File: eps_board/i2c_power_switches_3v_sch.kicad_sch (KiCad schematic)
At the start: 10 parts, among them U34 MCP23017T-E/SS

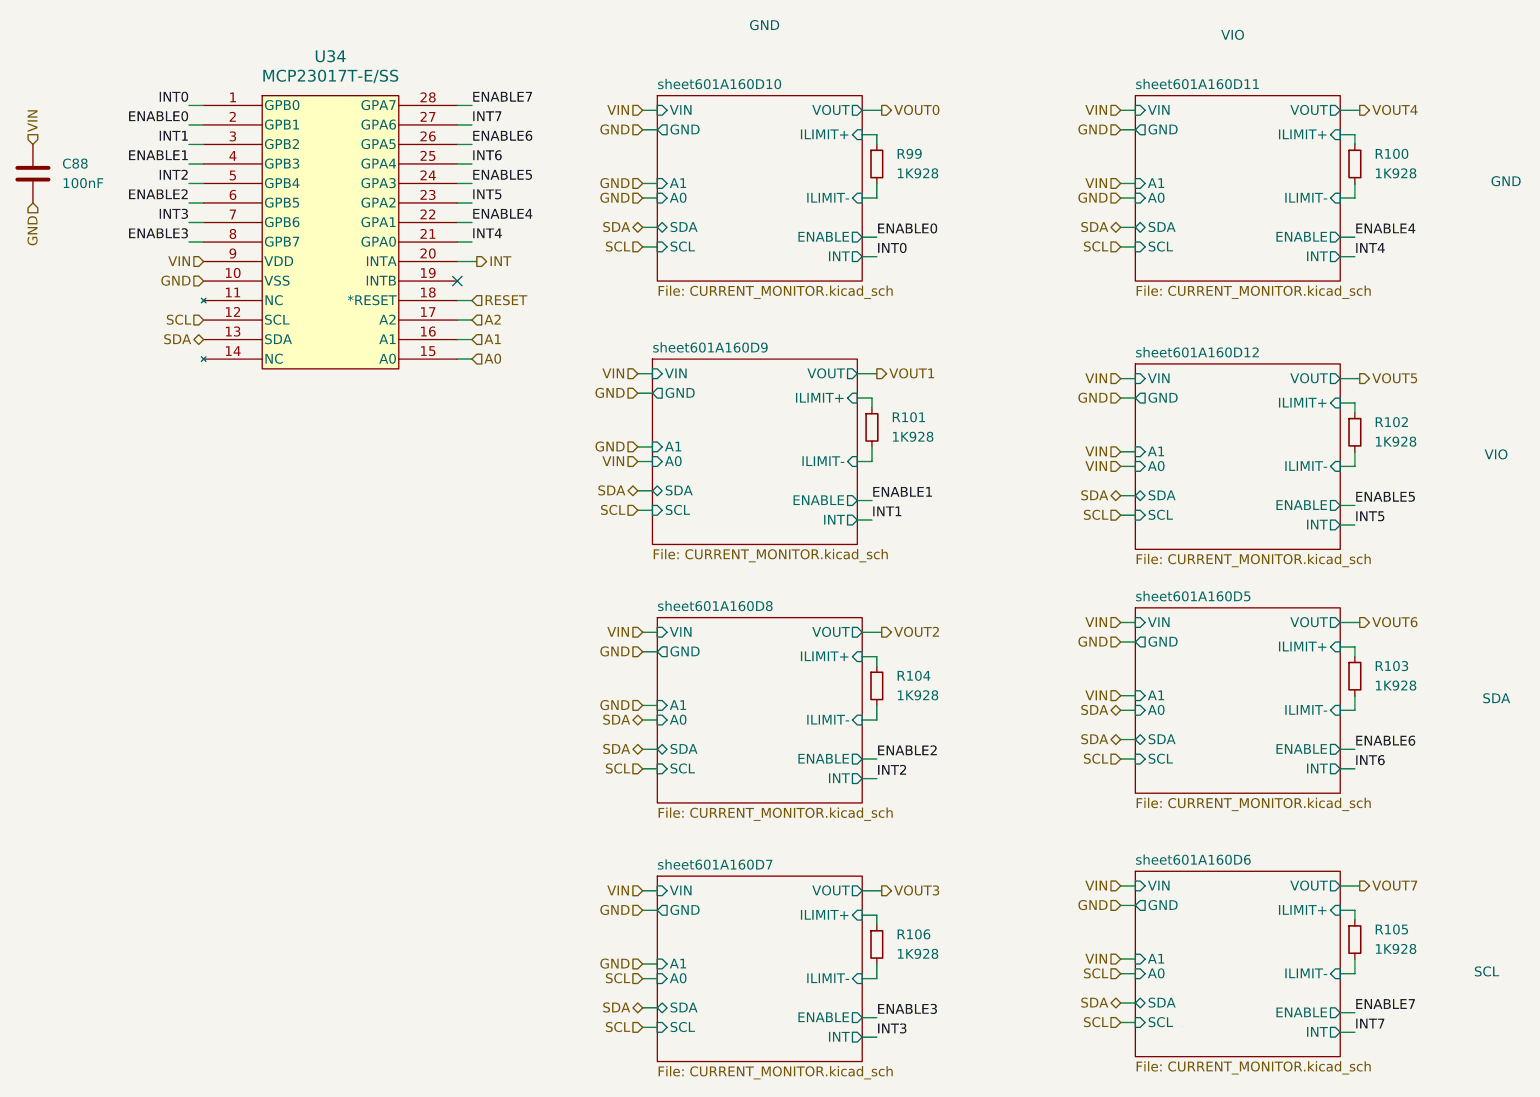
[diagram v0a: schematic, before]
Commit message: cleaning up bom: remove main camera port since it has not pullups and capacitors, correcting some errors in camera switch
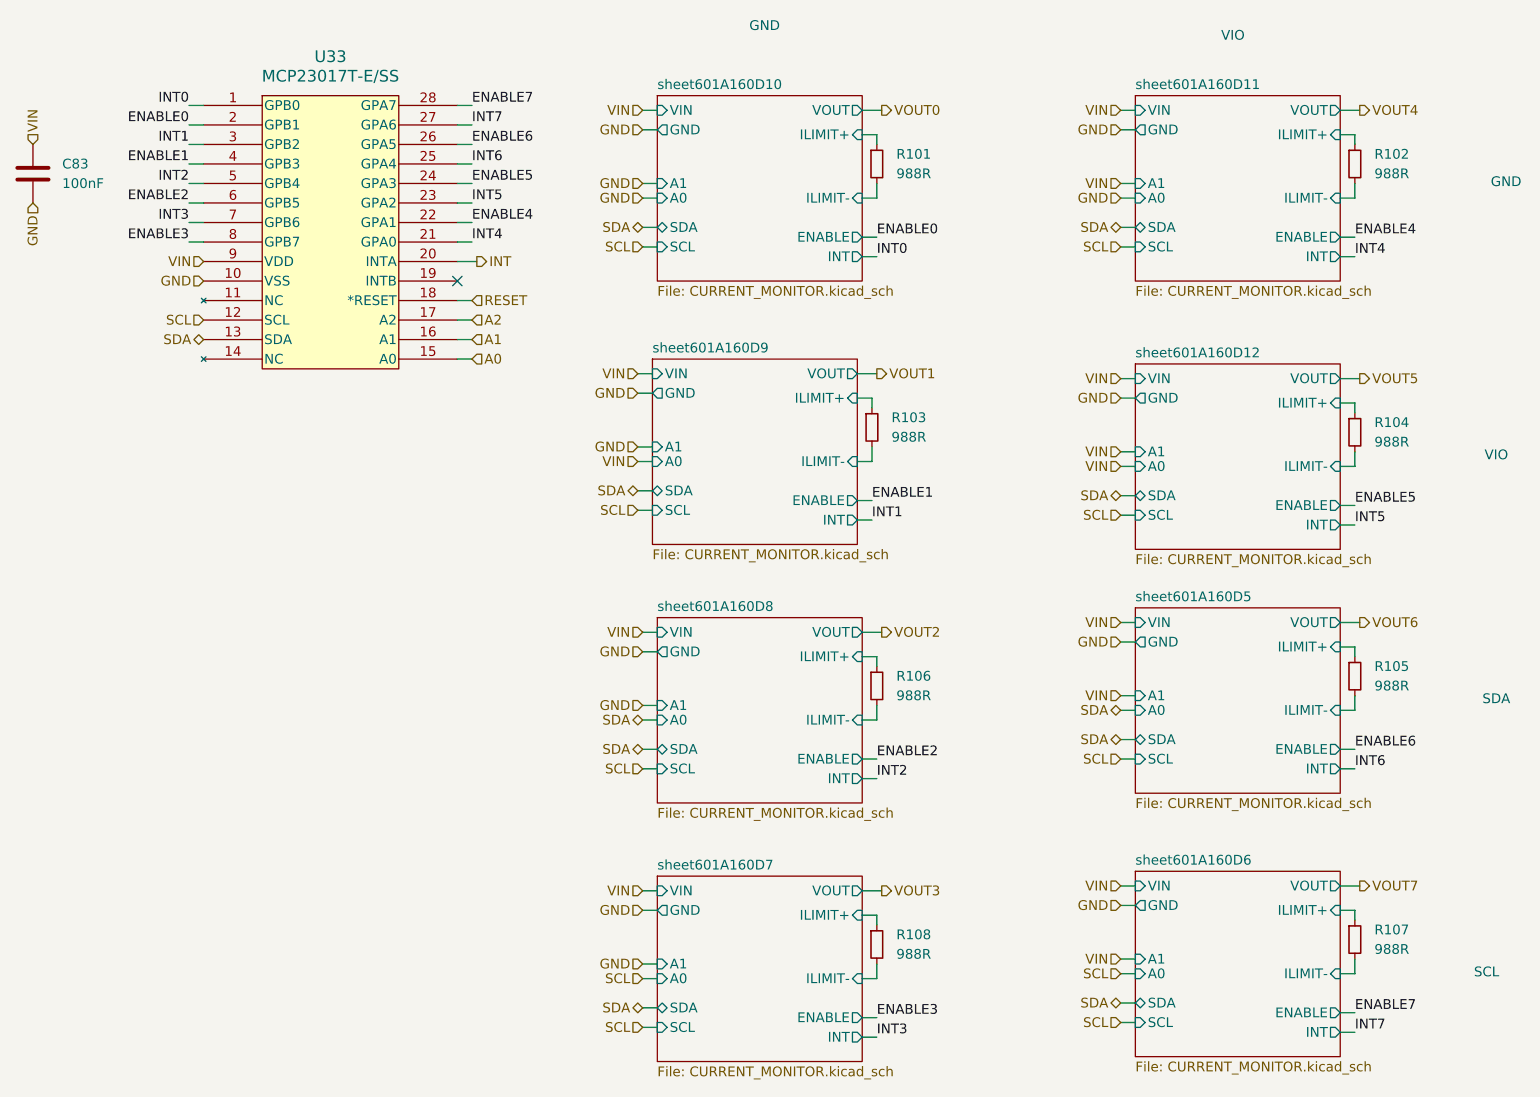
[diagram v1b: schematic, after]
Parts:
- R101: renamed from R99; value 1K928 -> 988R; Part Number RC0603FR-071K928L -> RT0603DRE07988RL; Tolerance 1 -> 0.5
- R102: renamed from R100; value 1K928 -> 988R; Part Number RC0603FR-071K928L -> RT0603DRE07988RL; Tolerance 1 -> 0.5
- R103: renamed from R101; value 1K928 -> 988R; Part Number RC0603FR-071K928L -> RT0603DRE07988RL; Tolerance 1 -> 0.5
- R104: renamed from R102; value 1K928 -> 988R; Part Number RC0603FR-071K928L -> RT0603DRE07988RL; Tolerance 1 -> 0.5
- R105: renamed from R103; value 1K928 -> 988R; Part Number RC0603FR-071K928L -> RT0603DRE07988RL; Tolerance 1 -> 0.5
- R106: renamed from R104; value 1K928 -> 988R; Part Number RC0603FR-071K928L -> RT0603DRE07988RL; Tolerance 1 -> 0.5
- R107: renamed from R105; value 1K928 -> 988R; Part Number RC0603FR-071K928L -> RT0603DRE07988RL; Tolerance 1 -> 0.5
- R108: renamed from R106; value 1K928 -> 988R; Part Number RC0603FR-071K928L -> RT0603DRE07988RL; Tolerance 1 -> 0.5
- renumbered C88 to C83, U34 to U33
